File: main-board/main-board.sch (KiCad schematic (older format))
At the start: 95 parts, among them J1 BOOT, J10 8P8CDouble, J11 Qwiic, J12 Qwiic, J13 Qwiic, J14 Micro_SD_Card_Det, J15 Interrupts1, J16 Interrupts2, J2 USB Header, J3 JTAG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

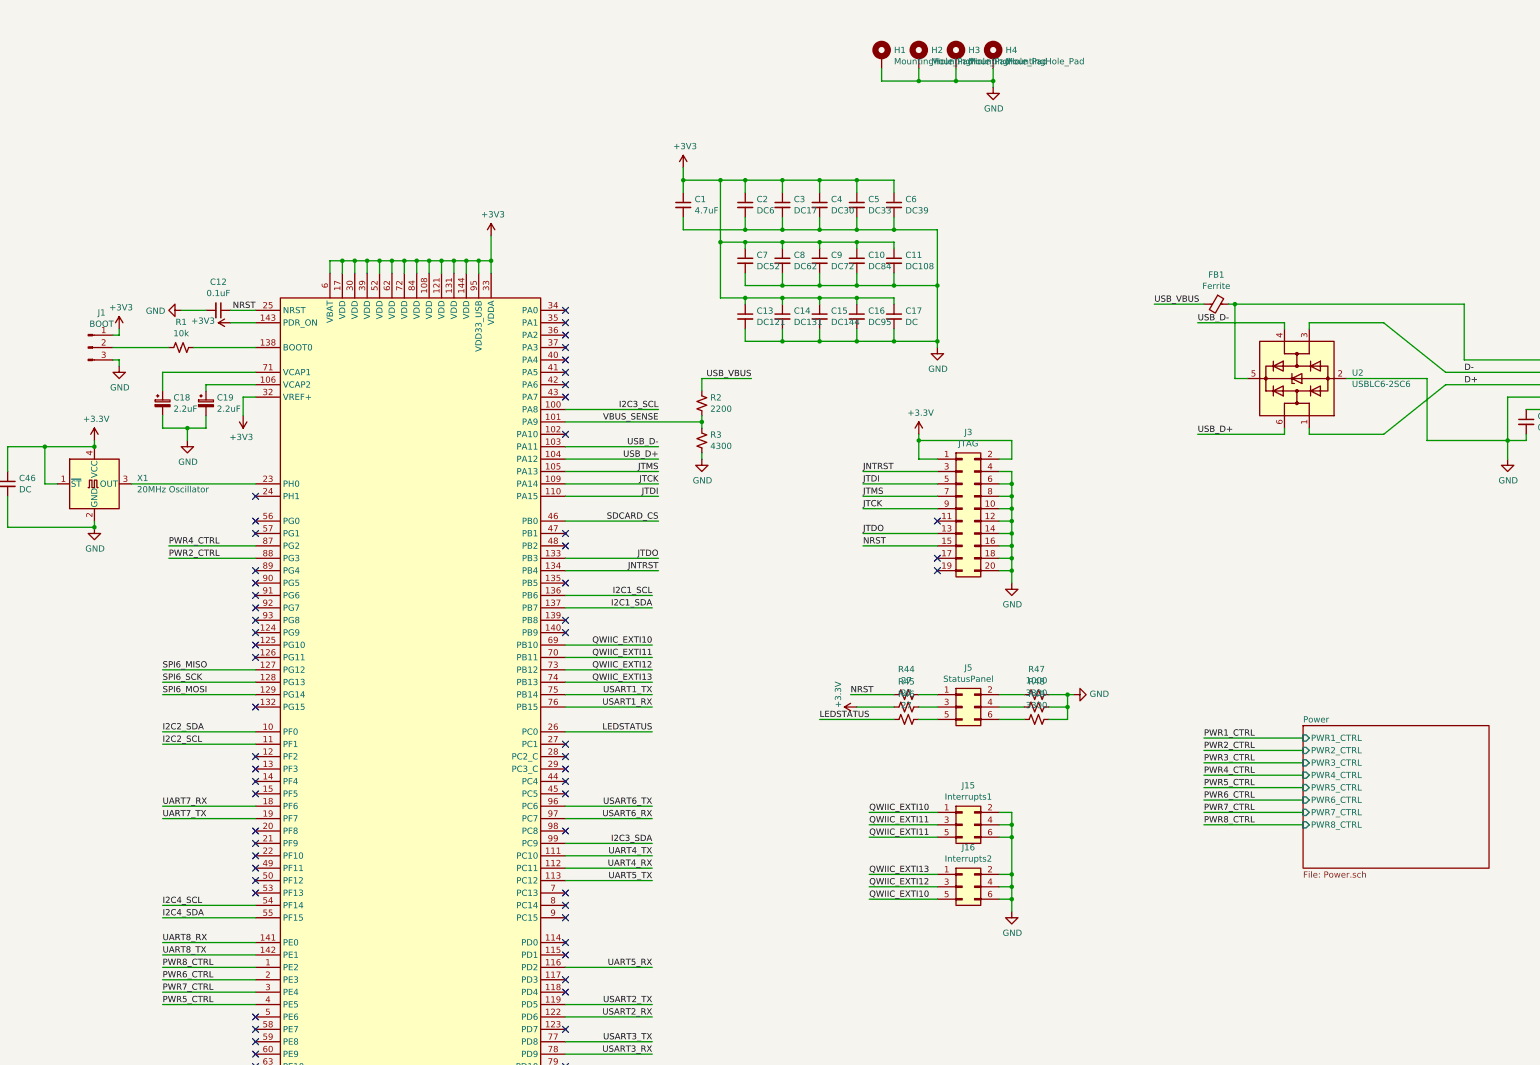
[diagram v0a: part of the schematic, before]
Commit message: Add RTC oscillator, battery header and LDO
Also moved the boot pin to defaulting from flash.
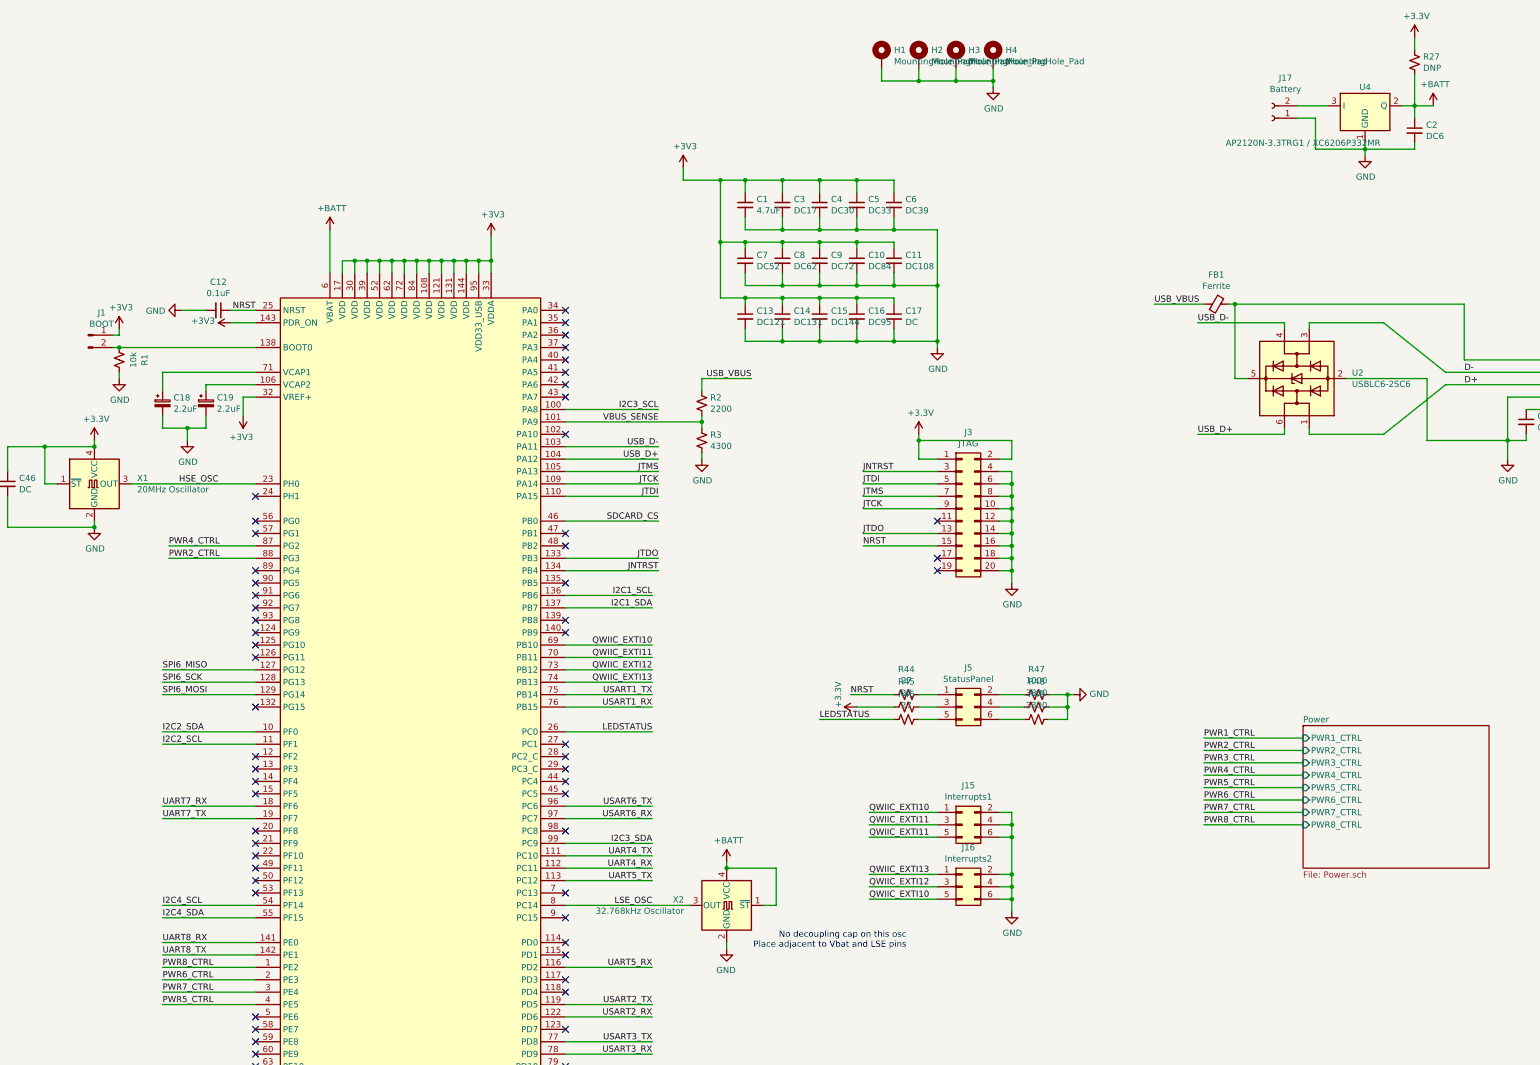
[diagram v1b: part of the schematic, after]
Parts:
- removed J1: BOOT, Pin_Headers:Pin_Header_Straight_1x03_Pitch2.54mm, symbol Connector:Conn_01x03_Male
- added J1: BOOT, Pin_Headers:Pin_Header_Straight_1x02_Pitch2.54mm, symbol Connector:Conn_01x02_Male
- added J17: Battery, Connectors_JST:JST_PH_B2B-PH-SM4-TB_02x2.00mm_Straight, symbol Connector:Conn_01x02_Female
- added R27: DNP, Resistors_SMD:R_0805_HandSoldering, symbol Device:R_Small_US
- added U4: AP2120N-3.3TRG1 / XC6206P332MR, TO_SOT_Packages_SMD:SOT-23, symbol Regulator_Linear:IFX27001TFV15
- added X2: 32.768kHz Oscillator, Oscillators:Oscillator_SMD_SeikoEpson_SG8002CE-4pin_3.2x2.5mm_HandSoldering, symbol Oscillator:SG-5032CAN
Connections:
- net +3V3: now also J1.1 (Pin_1), R27.1; no longer C2.1, U1.6 (VBAT)
- net GND: now also R1.1, J17.1 (Pin_1), U4.1 (GND), X2.2 (GND)
- net at U1.138 (BOOT0): now also R1.2, J1.2 (Pin_2); no longer R1.1
- net HSE_OSC: now reaches U1.23 (PH0), X1.3 (OUT)
- net LSE_OSC: now reaches U1.8 (PC14)
- net LSE_OSC: now also X2.3 (OUT)
- new net: J17.2 (Pin_2), U4.3 (I)
- new net +BATT: C2.1, R27.2, U1.6 (VBAT), U4.2 (Q), X2.1 (~ST), X2.4 (VCC)
- no-connect marks 69 -> 68
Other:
- note added: "No decoupling cap on this osc\nPlace adjacent to Vbat and LSE pins"
- moved on the sheet: C1, C2, R1
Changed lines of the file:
@@
 	12550 2700 12450 2700
 Wire Wire Line
-	11250 2700 11250 2800
-Wire Wire Line
 	11350 2800 11350 2700
-Connection ~ 11350 2700
-Wire Wire Line
-	11350 2700 11250 2700
 Wire Wire Line
 	11450 2800 11450 2700
@@
 L Device:C_Small C1
 U 1 1 5FC42E43
-P 14100 2250
-F 0 "C1" H 14192 2296 50  0000 L CNN
-F 1 "4.7uF" H 14192 2205 50  0000 L CNN
-F 2 "Capacitors_SMD:C_0805" H 14100 2250 50  0001 C CNN
-F 3 "~" H 14100 2250 50  0001 C CNN
-	1    14100 2250
+P 14600 2250
+F 0 "C1" H 14692 2296 50  0000 L CNN
+F 1 "4.7uF" H 14692 2205 50  0000 L CNN
+F 2 "Capacitors_SMD:C_0805" H 14600 2250 50  0001 C CNN
+F 3 "~" H 14600 2250 50  0001 C CNN
+	1    14600 2250
 	1    0    0    -1
 $EndComp
@@
 L Device:C_Small C2
 U 1 1 5FC43CD5
-P 14600 2250
-F 0 "C2" H 14692 2296 50  0000 L CNN
-F 1 "DC6" H 14692 2205 50  0000 L CNN
-F 2 "Capacitors_SMD:C_0805" H 14600 2250 50  0001 C CNN
-F 3 "~" H 14600 2250 50  0001 C CNN
-	1    14600 2250
+P 20000 1650
+F 0 "C2" H 20092 1696 50  0000 L CNN
+F 1 "DC6" H 20092 1605 50  0000 L CNN
+F 2 "Capacitors_SMD:C_0805" H 20000 1650 50  0001 C CNN
+F 3 "~" H 20000 1650 50  0001 C CNN
+	1    20000 1650
 	1    0    0    -1
 $EndComp
@@
 Wire Wire Line
 	15800 2050 15800 2150
-Connection ~ 14100 2050
-Wire Wire Line
-	14100 2050 14100 2150
 Wire Wire Line
 	15500 2150 15500 2050
@@
 	15500 3000 15200 3000
 Wire Wire Line
-	14100 2350 14100 2450
-Wire Wire Line
-	14100 2450 14600 2450
-Wire Wire Line
 	16150 2450 16150 2900
 Wire Wire Line
 	14600 2450 14600 2350
-Connection ~ 14600 2450
 Wire Wire Line
 	14600 2450 14900 2450
@@
 	10450 3200 10650 3200
 $Comp
-L Connector:Conn_01x03_Male J1
-U 1 1 5FDE10C0
-P 9300 3400
-F 0 "J1" H 9408 3681 50  0000 C CNN
-F 1 "BOOT" H 9408 3590 50  0000 C CNN
-F 2 "Pin_Headers:Pin_Header_Straight_1x03_Pitch2.54mm" H 9300 3400 50  0001 C CNN
-F 3 "~" H 9300 3400 50  0001 C CNN
-	1    9300 3400
-	1    0    0    -1
-$EndComp
-$Comp
 L Device:R_Small_US R1
 U 1 1 5FDE1D92
-P 10050 3400
-F 0 "R1" V 9845 3400 50  0000 C CNN
-F 1 "10k" V 9936 3400 50  0000 C CNN
-F 2 "Resistors_SMD:R_0805" H 10050 3400 50  0001 C CNN
-F 3 "~" H 10050 3400 50  0001 C CNN
-	1    10050 3400
-	0    1    1    0
+P 9550 3500
+F 0 "R1" V 9345 3500 50  0000 C CNN
+F 1 "10k" V 9436 3500 50  0000 C CNN
+F 2 "Resistors_SMD:R_0805" H 9550 3500 50  0001 C CNN
+F 3 "~" H 9550 3500 50  0001 C CNN
+	1    9550 3500
+	-1   0    0    1
 $EndComp
 Wire Wire Line
-	10650 3400 10150 3400
-Wire Wire Line
-	9950 3400 9500 3400
+	9550 3400 9500 3400
 $Comp
 L power:GND #PWR0109
 U 1 1 5FDF3211
-P 9550 3550
-F 0 "#PWR0109" H 9550 3300 50  0001 C CNN
-F 1 "GND" H 9555 3377 50  0000 C CNN
-F 2 "" H 9550 3550 50  0001 C CNN
-F 3 "" H 9550 3550 50  0001 C CNN
-	1    9550 3550
+P 9550 3650
+F 0 "#PWR0109" H 9550 3400 50  0001 C CNN
+F 1 "GND" H 9555 3477 50  0000 C CNN
+F 2 "" H 9550 3650 50  0001 C CNN
+F 3 "" H 9550 3650 50  0001 C CNN
+	1    9550 3650
 	1    0    0    -1
 $EndComp
@@
 	9550 3300 9500 3300
 Wire Wire Line
-	9500 3500 9550 3500
-Wire Wire Line
-	9550 3500 9550 3550
+	9550 3600 9550 3650
 $Comp
 L Device:Ferrite_Bead_Small FB1
@@
 NoConn ~ 13150 8900
 NoConn ~ 13150 7800
-NoConn ~ 13150 7900
 NoConn ~ 13150 8000
 NoConn ~ 13150 8200
@@
 Text Label 15600 7850 0    50   ~ 0
 QWIIC_EXTI10
+Text Label 10350 4500 2    50   ~ 0
+HSE_OSC
+$Comp
+L Oscillator:SG-5032CAN X2
+U 1 1 604AF004
+P 14450 7900
+F 0 "X2" H 14794 7946 50  0000 L CNN
+F 1 "32.768kHz Oscillator" H 14794 7855 50  0000 L CNN
+F 2 "Oscillators:Oscillator_SMD_SeikoEpson_SG8002CE-4pin_3.2x2.5mm_HandSoldering" H 15150 7550 50  0001 C CNN
+F 3 "https://support.epson.biz/td/api/doc_check.php?dl=brief_SG5032CAN&lang=en" H 14350 7900 50  0001 C CNN
+	1    14450 7900
+	-1   0    0    -1
+$EndComp
+$Comp
+L power:GND #PWR0135
+U 1 1 604AF010
+P 14450 8250
+F 0 "#PWR0135" H 14450 8000 50  0001 C CNN
+F 1 "GND" H 14455 8077 50  0000 C CNN
+F 2 "" H 14450 8250 50  0001 C CNN
+F 3 "" H 14450 8250 50  0001 C CNN
+	1    14450 8250
+	-1   0    0    -1
+$EndComp
+Wire Wire Line
+	14450 7550 14450 7600
+Wire Wire Line
+	14450 8200 14450 8250
+Wire Wire Line
+	14150 7900 13150 7900
+Wire Wire Line
+	14750 7900 14850 7900
+Wire Wire Line
+	14850 7900 14850 7600
+Wire Wire Line
+	14850 7600 14450 7600
+Connection ~ 14450 7600
+Text Label 13850 7900 2    50   ~ 0
+LSE_OSC
+$Comp
+L power:+BATT #PWR0136
+U 1 1 605ADD80
+P 14450 7550
+F 0 "#PWR0136" H 14450 7400 50  0001 C CNN
+F 1 "+BATT" H 14465 7723 50  0000 C CNN
+F 2 "" H 14450 7550 50  0001 C CNN
+F 3 "" H 14450 7550 50  0001 C CNN
+	1    14450 7550
+	1    0    0    -1
+$EndComp
+$Comp
+L power:+BATT #PWR0137
+U 1 1 605AF084
+P 11250 2450
+F 0 "#PWR0137" H 11250 2300 50  0001 C CNN
+F 1 "+BATT" H 11265 2623 50  0000 C CNN
+F 2 "" H 11250 2450 50  0001 C CNN
+F 3 "" H 11250 2450 50  0001 C CNN
+	1    11250 2450
+	1    0    0    -1
+$EndComp
+Wire Wire Line
+	19900 1450 20000 1450
+$Comp
+L power:+BATT #PWR0138
+U 1 1 607A7C17
+P 20150 1450
+F 0 "#PWR0138" H 20150 1300 50  0001 C CNN
+F 1 "+BATT" H 20165 1623 50  0000 C CNN
+F 2 "" H 20150 1450 50  0001 C CNN
+F 3 "" H 20150 1450 50  0001 C CNN
+	1    20150 1450
+	1    0    0    -1
+$EndComp
+$Comp
+L Regulator_Linear:IFX27001TFV15 U4
+U 1 1 607A87DC
+P 19600 1450
+F 0 "U4" H 19600 1600 50  0000 C CNN
+F 1 "AP2120N-3.3TRG1 / XC6206P332MR" H 19100 1150 50  0000 C CNN
+F 2 "TO_SOT_Packages_SMD:SOT-23" H 19600 1400 50  0001 C CNN
+F 3 "https://static6.arrow.com/aropdfconversion/dc75757ae45a88e5f69bdce3f2a651a5fe0ca07d/ifx27001_ds_10.pdf" H 19600 1400 50  0001 C CNN
+	1    19600 1450
+	1    0    0    -1
+$EndComp
+$Comp
+L power:GND #PWR0139
+U 1 1 607AA5E1
+P 19600 1850
+F 0 "#PWR0139" H 19600 1600 50  0001 C CNN
+F 1 "GND" H 19605 1677 50  0000 C CNN
+F 2 "" H 19600 1850 50  0001 C CNN
+F 3 "" H 19600 1850 50  0001 C CNN
+	1    19600 1850
+	1    0    0    -1
+$EndComp
+Wire Wire Line
+	19600 1850 19600 1800
+Wire Wire Line
+	11250 2450 11250 2800
+Wire Wire Line
+	19600 1800 20000 1800
+Wire Wire Line
+	20000 1800 20000 1750
+Connection ~ 19600 1800
+Wire Wire Line
+	19600 1800 19600 1750
+Wire Wire Line
+	20000 1550 20000 1450
+Connection ~ 20000 1450
+Wire Wire Line
+	20000 1450 20150 1450
+$Comp
+L Device:R_Small_US R27
+U 1 1 6091C49E
+P 20000 1100
+F 0 "R27" H 20068 1146 50  0000 L CNN
+F 1 "DNP" H 20068 1055 50  0000 L CNN
+F 2 "Resistors_SMD:R_0805_HandSoldering" H 20000 1100 50  0001 C CNN
+F 3 "~" H 20000 1100 50  0001 C CNN
+	1    20000 1100
+	1    0    0    -1
+$EndComp
+$Comp
+L power:+3.3V #PWR0187
+U 1 1 6091D87B
+P 20000 900
+F 0 "#PWR0187" H 20000 750 50  0001 C CNN
+F 1 "+3.3V" H 20015 1073 50  0000 C CNN
+F 2 "" H 20000 900 50  0001 C CNN
+F 3 "" H 20000 900 50  0001 C CNN
+	1    20000 900
+	1    0    0    -1
+$EndComp
+Wire Wire Line
+	20000 900  20000 1000
+Wire Wire Line
+	20000 1200 20000 1450
+$Comp
+L Connector:Conn_01x02_Female J17
+U 1 1 60A170C9
+P 18850 1550
+F 0 "J17" H 18742 1225 50  0000 C CNN
+F 1 "Battery" H 18742 1316 50  0000 C CNN
+F 2 "Connectors_JST:JST_PH_B2B-PH-SM4-TB_02x2.00mm_Straight" H 18850 1550 50  0001 C CNN
+F 3 "~" H 18850 1550 50  0001 C CNN
+	1    18850 1550
+	-1   0    0    1
+$EndComp
+Wire Wire Line
+	19050 1550 19200 1550
+Wire Wire Line
+	19200 1550 19200 1800
+Wire Wire Line
+	19200 1800 19600 1800
+Wire Wire Line
+	19050 1450 19300 1450
+Text Notes 15900 8250 2    50   ~ 0
+No decoupling cap on this osc\nPlace adjacent to Vbat and LSE pins
+$Comp
+L Connector:Conn_01x02_Male J1
+U 1 1 60C0234F
+P 9300 3300
+F 0 "J1" H 9408 3481 50  0000 C CNN
+F 1 "BOOT" H 9408 3390 50  0000 C CNN
+F 2 "Pin_Headers:Pin_Header_Straight_1x02_Pitch2.54mm" H 9300 3300 50  0001 C CNN
+F 3 "~" H 9300 3300 50  0001 C CNN
+	1    9300 3300
+	1    0    0    -1
+$EndComp
+Wire Wire Line
+	9550 3400 10650 3400
+Connection ~ 9550 3400
 $EndSCHEMATC

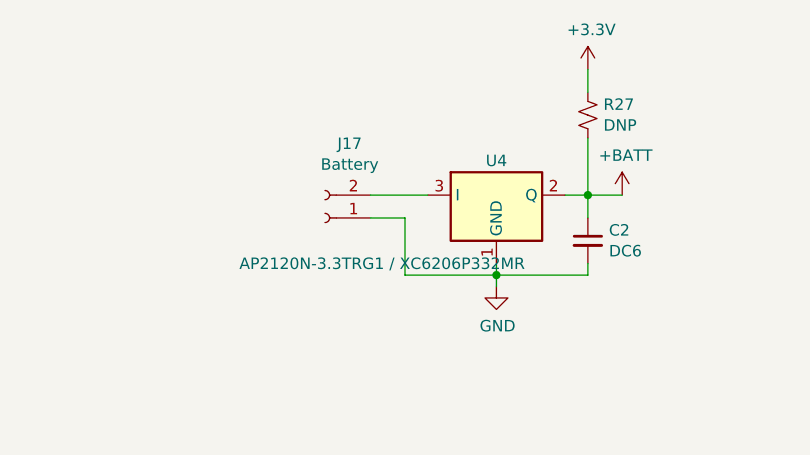
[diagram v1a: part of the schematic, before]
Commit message: Tweak a bunch of traces, bump the board rev
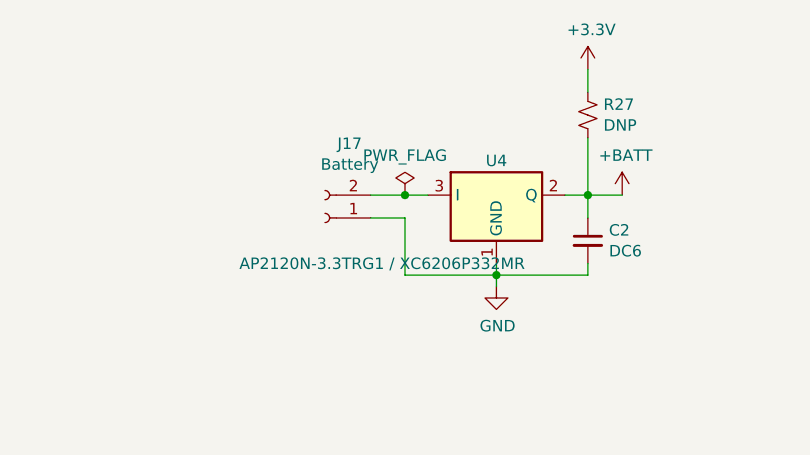
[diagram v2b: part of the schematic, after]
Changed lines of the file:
@@
 	19200 1800 19600 1800
 Wire Wire Line
-	19050 1450 19300 1450
+	19050 1450 19200 1450
 Text Notes 15900 8250 2    50   ~ 0
 No decoupling cap on this osc\nPlace adjacent to Vbat and LSE pins
@@
 	9550 3400 10650 3400
 Connection ~ 9550 3400
+$Comp
+L power:PWR_FLAG #FLG0101
+U 1 1 60118BE6
+P 19200 1450
+F 0 "#FLG0101" H 19200 1525 50  0001 C CNN
+F 1 "PWR_FLAG" H 19200 1623 50  0000 C CNN
+F 2 "" H 19200 1450 50  0001 C CNN
+F 3 "~" H 19200 1450 50  0001 C CNN
+	1    19200 1450
+	1    0    0    -1
+$EndComp
+Connection ~ 19200 1450
+Wire Wire Line
+	19200 1450 19300 1450
 $EndSCHEMATC
